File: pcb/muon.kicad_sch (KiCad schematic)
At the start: 16 parts, among them J1 Debug Pins, J2 USB_C_Receptacle_USB2.0, SW1 SW_SPST, SW2 SW_SPST, U1 ATSAMD11C14A-SS, U2 MIC5528-3.3YMT-TR

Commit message: re-route traces for pretty
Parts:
- added D2, D3: LED_RGBA, footprints:156120M173000, symbol Device:LED_RGBA
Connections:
- net +3V3: now also D2.4 (A), D3.4 (A)
- net SW1: now also U1.5 (PA15); no longer U1.4 (PA14)
- net SW2: now also U1.4 (PA14); no longer U1.5 (PA15)
- net LED_B: now reaches U1.1 (PA05)
- net LED_B: now also D2.3 (BK), D3.3 (BK)
- net LED_G: now reaches U1.2 (PA08/XIN)
- net LED_G: now also D2.2 (GK), D3.2 (GK)
- net LED_R: now reaches U1.3 (PA09/XOUT)
- net LED_R: now also D2.1 (RK), D3.1 (RK)

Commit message: re-route again
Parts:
- SW1, SW2: footprint Button_Switch_Keyboard:SW_Cherry_MX_1.25u_PCB -> Keyswitch:SW_Hotswap_Kailh_MX_1.25u
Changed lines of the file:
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@@
     (property "Reference" "SW2" (id 0) (at 193.04 101.6 0))
     (property "Value" "SW_SPST" (id 1) (at 200.66 87.63 0))
-    (property "Footprint" "Button_Switch_Keyboard:SW_Cherry_MX_1.25u_PCB" (id 2) (at 193.04 97.79 0)
+    (property "Footprint" "Keyswitch:SW_Hotswap_Kailh_MX_1.25u" (id 2) (at 193.04 97.79 0)
       (effects (font (size 1.27 1.27)) hide)
     )
@@
     (property "Reference" "SW1" (id 0) (at 193.04 90.17 0))
     (property "Value" "SW_SPST" (id 1) (at 200.66 87.63 0))
-    (property "Footprint" "Button_Switch_Keyboard:SW_Cherry_MX_1.25u_PCB" (id 2) (at 193.04 93.98 0)
+    (property "Footprint" "Keyswitch:SW_Hotswap_Kailh_MX_1.25u" (id 2) (at 193.04 93.98 0)
       (effects (font (size 1.27 1.27)) hide)
     )
@@
     )
     (path "/a27ad806-2f49-493b-a712-5cefb34fea4e"
-      (reference "SW1") (unit 1) (value "SW_SPST") (footprint "Button_Switch_Keyboard:SW_Cherry_MX_1.25u_PCB")
+      (reference "SW1") (unit 1) (value "SW_SPST") (footprint "Keyswitch:SW_Hotswap_Kailh_MX_1.25u")
     )
     (path "/80001a61-1fa4-4527-9790-681f063e52bc"
-      (reference "SW2") (unit 1) (value "SW_SPST") (footprint "Button_Switch_Keyboard:SW_Cherry_MX_1.25u_PCB")
+      (reference "SW2") (unit 1) (value "SW_SPST") (footprint "Keyswitch:SW_Hotswap_Kailh_MX_1.25u")
     )
     (path "/d0bfe201-daa4-4d35-9ccd-fa6a79ba80ae"

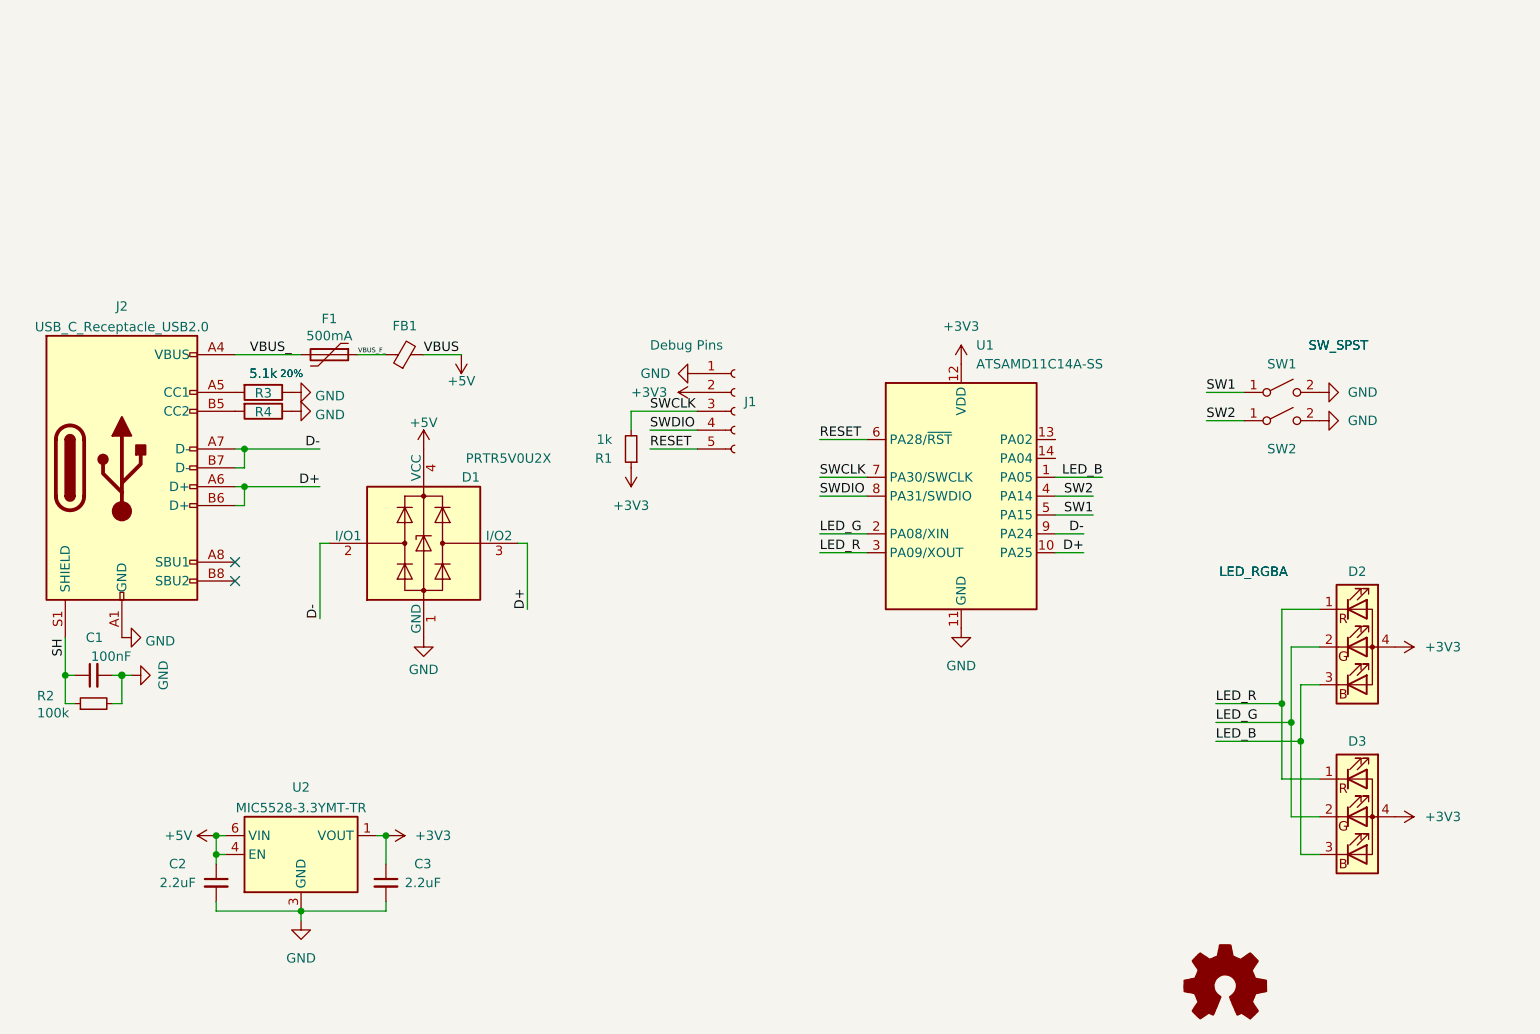
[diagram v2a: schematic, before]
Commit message: update schematic with proper parts
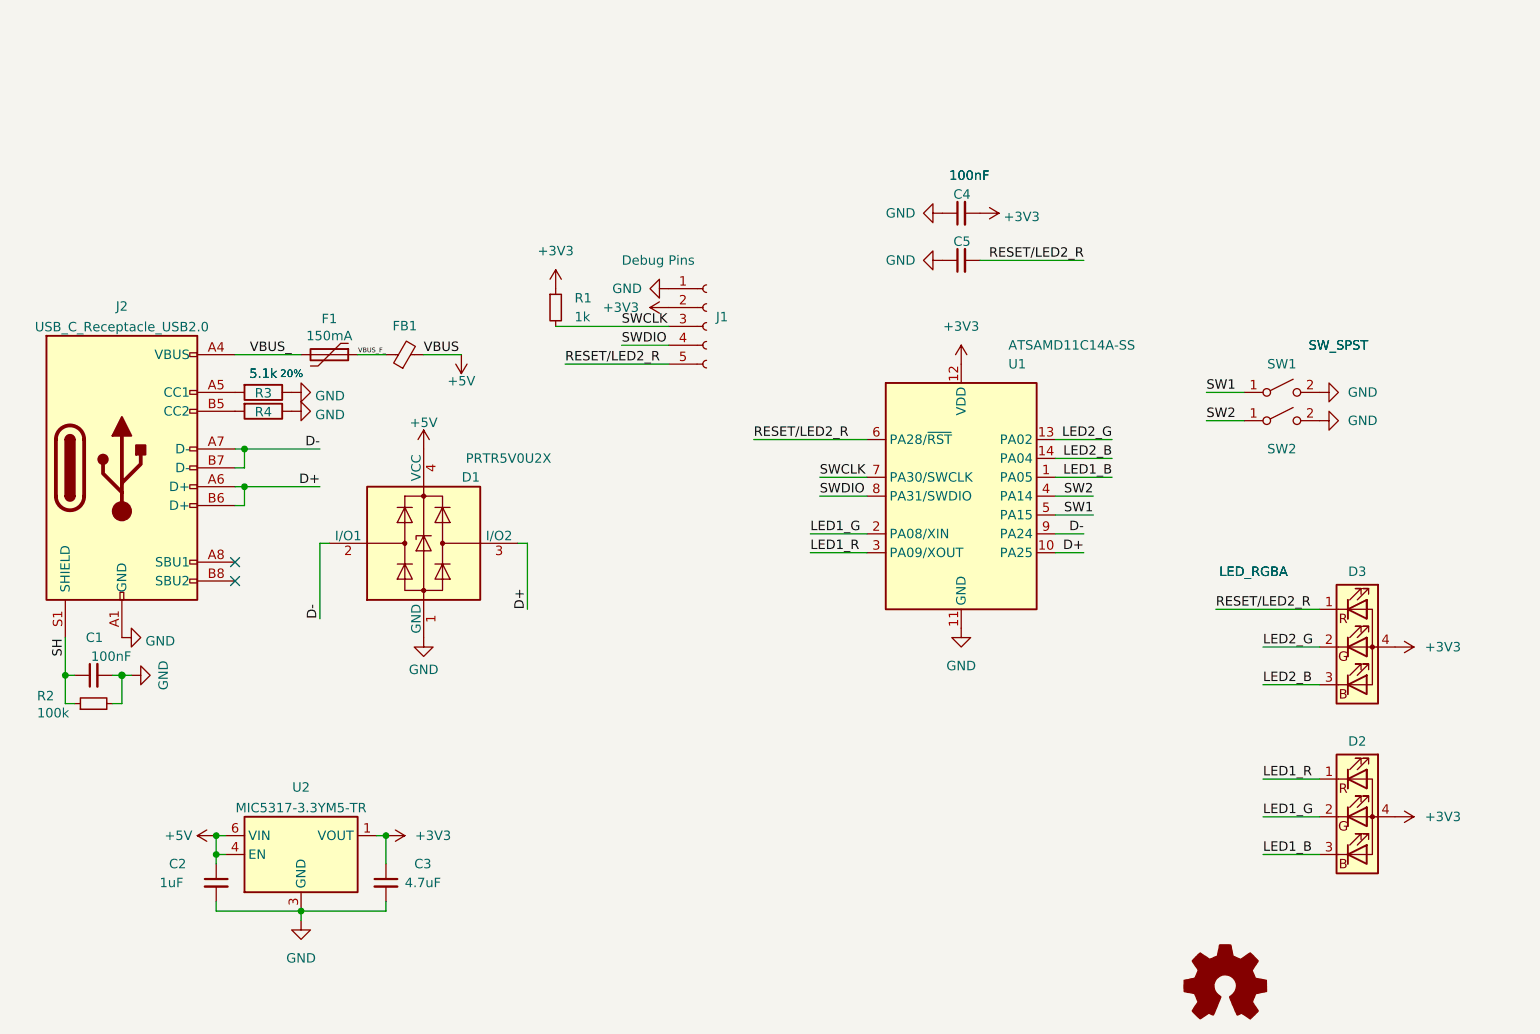
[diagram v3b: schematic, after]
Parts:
- added C4, C5: 100nF, Capacitor_SMD:C_0402_1005Metric, symbol Device:C_Small
- C2: value 2.2uF -> 1uF
- C3: value 2.2uF -> 4.7uF
- F1: value 500mA -> 150mA
- U2: value MIC5528-3.3YMT-TR -> MIC5317-3.3YM5-TR; footprint MIC55:SON40P120X120X60-7N -> Package_TO_SOT_SMD:SOT-23-5_HandSoldering
- renumbered D3 to D2, D2 to D3
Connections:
- net +3V3: now also C4.2
- net GND: now also C4.1, C5.1
- net LED2_G: now reaches U1.13 (PA02)
- net LED2_G: now also D3.2 (GK)
- net LED2_B: now reaches U1.14 (PA04)
- net LED2_B: now also D3.3 (BK)
- net LED_B renamed LED1_B
- net LED1_B: no longer D3.3 (BK)
- net LED_G renamed LED1_G
- net LED1_G: no longer D3.2 (GK)
- net LED_R renamed LED1_R
- net LED1_R: no longer D3.1 (RK)
- net RESET renamed RESET/LED2_R
- net RESET/LED2_R: now also D3.1 (RK), C5.2
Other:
- moved on the sheet: J1, R1

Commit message: re-route and remove 'uneeded' things
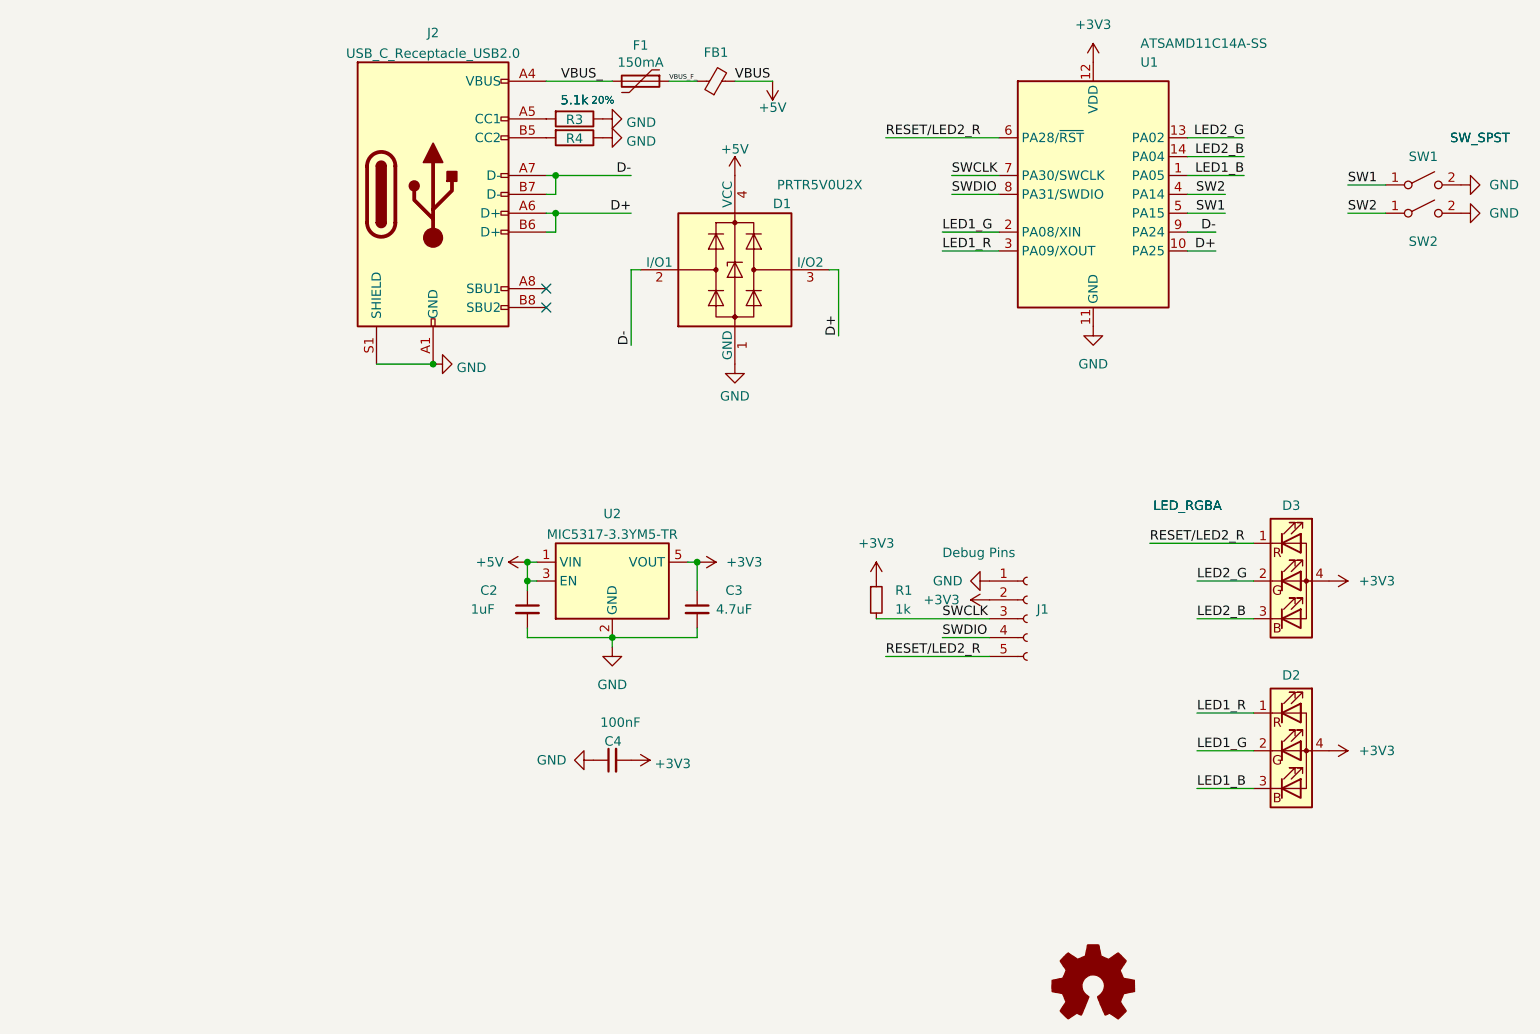
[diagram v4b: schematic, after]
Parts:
- removed C1, C5: 100nF, Capacitor_SMD:C_0402_1005Metric, symbol Device:C_Small
- removed R2: 100k, Resistor_SMD:R_0402_1005Metric, symbol Device:R_Small
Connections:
- net SH is gone; now on net GND: J2.S1 (SHIELD)
- net +3V3: now also U2.5 (VOUT); no longer U2.1 (VOUT), U2.2 (VOUT)
- net +5V: now also U2.1 (VIN), U2.3 (EN); no longer U2.4 (EN), U2.6 (VIN)
- net GND: now also U2.2 (GND); no longer U2.3 (GND)
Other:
- moved on the sheet: C2, C3, C4, D1, D2, D3, F1, FB1, J1, J2, R1, R3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

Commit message: post v0.1 quick fixes
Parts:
- C2: footprint Capacitor_SMD:C_0402_1005Metric -> Capacitor_SMD:C_0603_1608Metric
- R1: footprint Resistor_SMD:R_0603_1608Metric -> Resistor_SMD:R_0402_1005Metric
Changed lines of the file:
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@@
       (effects (font (size 1.27 1.27)) (justify left))
     )
-    (property "Footprint" "Resistor_SMD:R_0603_1608Metric" (id 2) (at 138.43 121.92 0)
+    (property "Footprint" "Resistor_SMD:R_0402_1005Metric" (id 2) (at 138.43 121.92 0)
       (effects (font (size 1.27 1.27)) hide)
     )
@@
       (effects (font (size 1.27 1.27)) (justify left))
     )
-    (property "Footprint" "Capacitor_SMD:C_0402_1005Metric" (id 2) (at 91.44 123.19 0)
+    (property "Footprint" "Capacitor_SMD:C_0603_1608Metric" (id 2) (at 91.44 123.19 0)
       (effects (font (size 1.27 1.27)) hide)
     )
@@
       (effects (font (size 1.27 1.27)) hide)
     )
+    (pin "1")
+    (pin "2")
+    (pin "3")
+    (pin "4")
     (pin "5")
-    (pin "3")
-    (pin "2")
-    (pin "4")
-    (pin "1")
   )
   (symbol (lib_id "power:GND") (at 217.17 69.85 90) (unit 1)
@@
     )
     (path "/593693bf-d6ae-4659-9e8b-ba22a0b5099d"
-      (reference "C2") (unit 1) (value "1uF") (footprint "Capacitor_SMD:C_0402_1005Metric")
+      (reference "C2") (unit 1) (value "1uF") (footprint "Capacitor_SMD:C_0603_1608Metric")
     )
     (path "/5582bf4e-99d4-4aaa-a0e4-5bbf4d0ed531"
@@
     )
     (path "/3afd2b2b-afb2-4823-a268-5ef1008a65c2"
-      (reference "R1") (unit 1) (value "1k") (footprint "Resistor_SMD:R_0603_1608Metric")
+      (reference "R1") (unit 1) (value "1k") (footprint "Resistor_SMD:R_0402_1005Metric")
     )
     (path "/3a8cb071-4bda-4fc9-8c8b-585e54604573"
